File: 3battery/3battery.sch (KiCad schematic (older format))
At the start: 61 parts, among them J1 Barrel_Jack, J2 1 cell, J3 3 cells, J4 opt, J5 opt, J6 opt, Q1 BSL302SNH6327XTSA1, Q2 BSL302SNH6327XTSA1, Q3 CPH6350-TL-W, U1 bq24133, U2 TPS62143

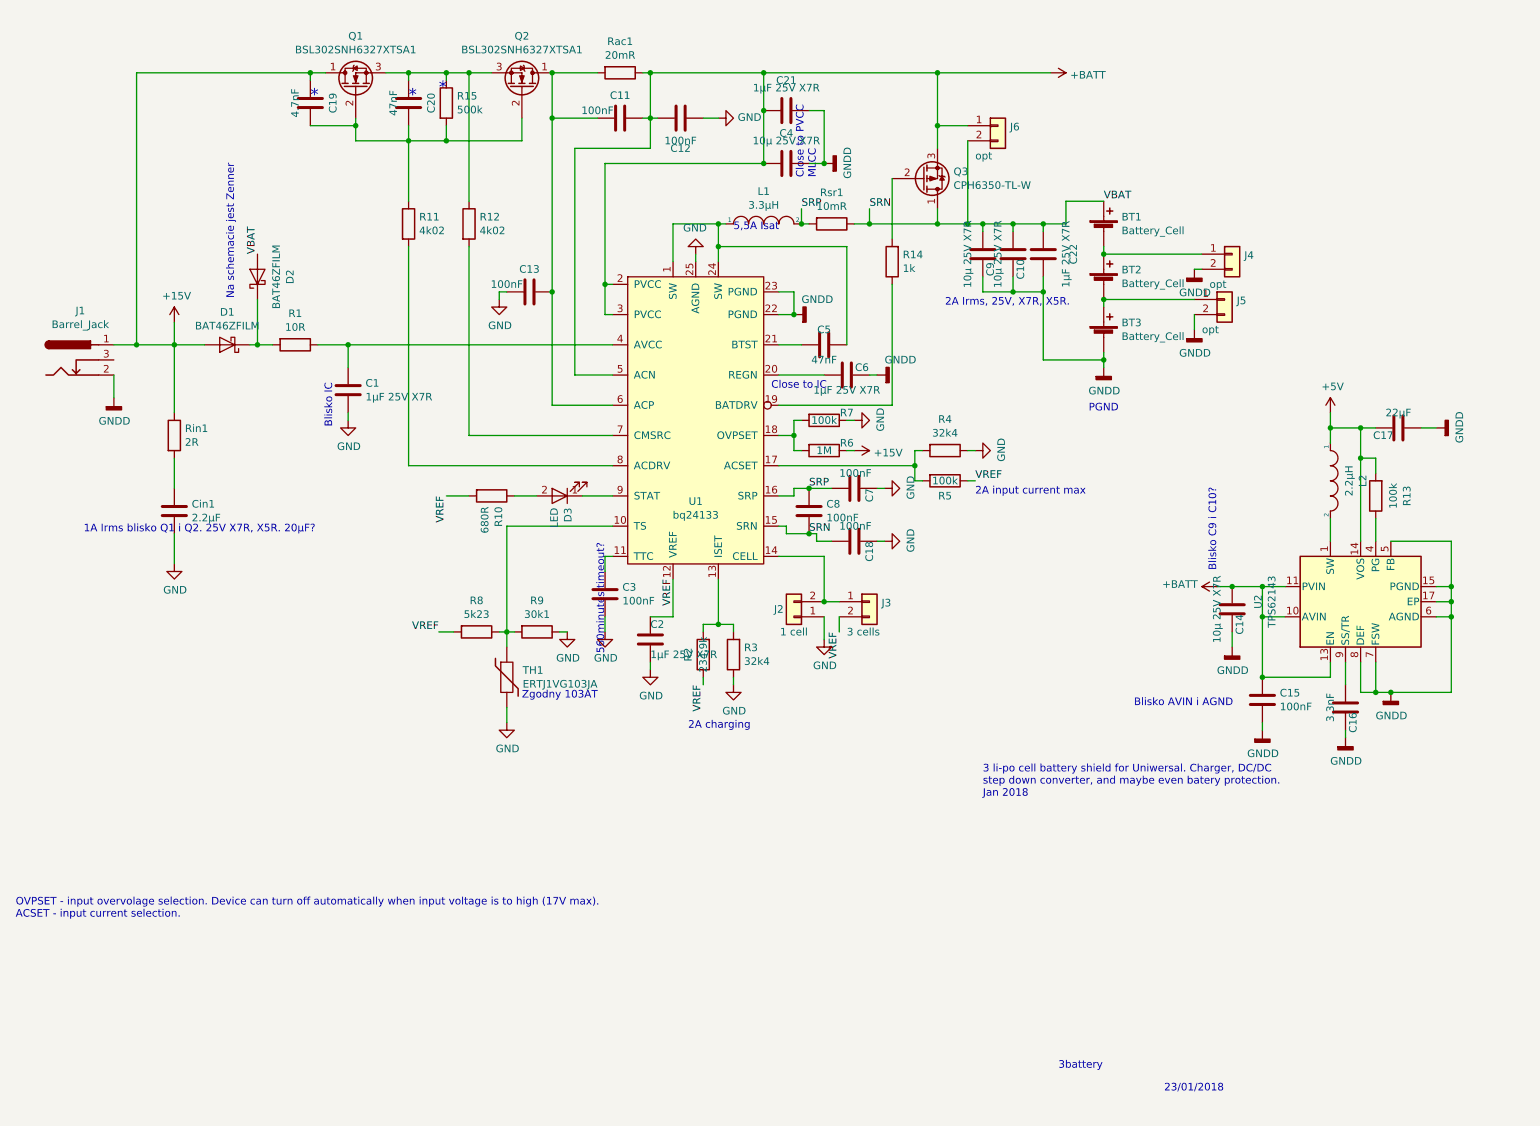
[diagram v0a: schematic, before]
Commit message: Main board and proto-board added
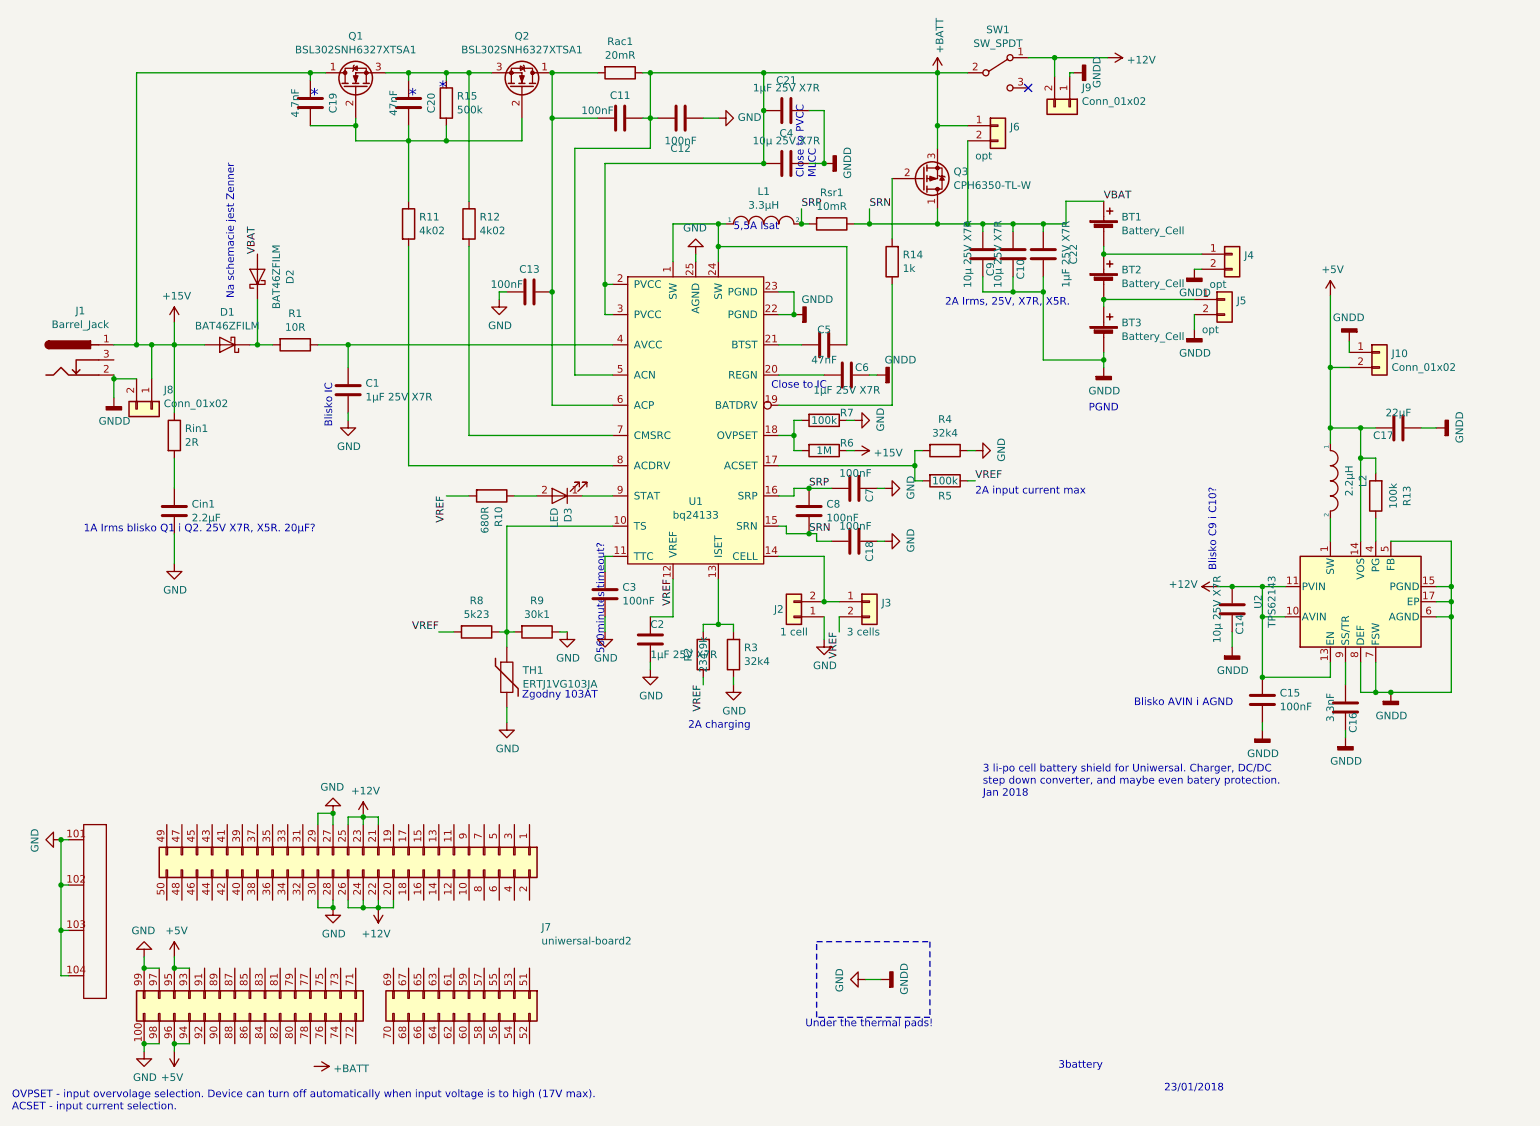
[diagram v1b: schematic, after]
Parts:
- added J10, J8, J9: Conn_01x02, Connector_PinHeader_2.54mm:PinHeader_1x02_P2.54mm_Vertical, symbol Connector_Generic:Conn_01x02
- added J7: uniwersal-board2, iwasz:uniwersal-board, symbol iwasz-kicad:uniwersal-board2
- added SW1: SW_SPDT, Button_Switch_THT:SW_CuK_OS102011MA1QN1_SPDT_Angled, symbol Switch:SW_SPDT
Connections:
- net GNDD is gone; now on net GND: BT3.2 (-), C10.1, C14.1, C15.2, C16.1, C17.2, C21.1, C22.1, C4.1, C6.1, C9.1, J1.2, J4.2 (Pin_2), J5.2 (Pin_2), U1.22 (PGND), U1.23 (PGND), U2.15 (PGND), U2.16 (PGND), U2.17 (EP), U2.5 (FB), U2.6 (AGND), U2.7 (FSW), U2.8 (DEF)
- net +15V: now also J8.1 (Pin_1)
- net +5V: now also J10.2 (Pin_2), J7.93 (Pin_23), J7.94 (Pin_24), J7.95 (Pin_25), J7.96 (Pin_26)
- net +BATT: now also SW1.2 (B); no longer C14.2, C15.1, U2.10 (AVIN), U2.11 (PVIN), U2.12 (PVIN), U2.13 (EN)
- net GND: now also J10.1 (Pin_1), J7.100 (Pin_30), J7.101, J7.102, J7.103, J7.104, J7.27 (Pin_27), J7.28 (Pin_28), J7.29 (Pin_29), J7.30 (Pin_30), J7.97 (Pin_27), J7.98 (Pin_28), J7.99 (Pin_29), J8.2 (Pin_2), J9.1 (Pin_1)
- new net +12V: C14.2, C15.1, J7.20 (Pin_20), J7.21 (Pin_21), J7.22 (Pin_22), J7.23 (Pin_23), J7.24 (Pin_24), J7.25 (Pin_25), J7.26 (Pin_26), J9.2 (Pin_2), SW1.1 (A), U2.10 (AVIN), U2.11 (PVIN), U2.12 (PVIN), U2.13 (EN)
- no-connect marks 0 -> 1
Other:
- note added: "Under the thermal pads!"

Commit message: Gerbers directory added, and domcumentation improved
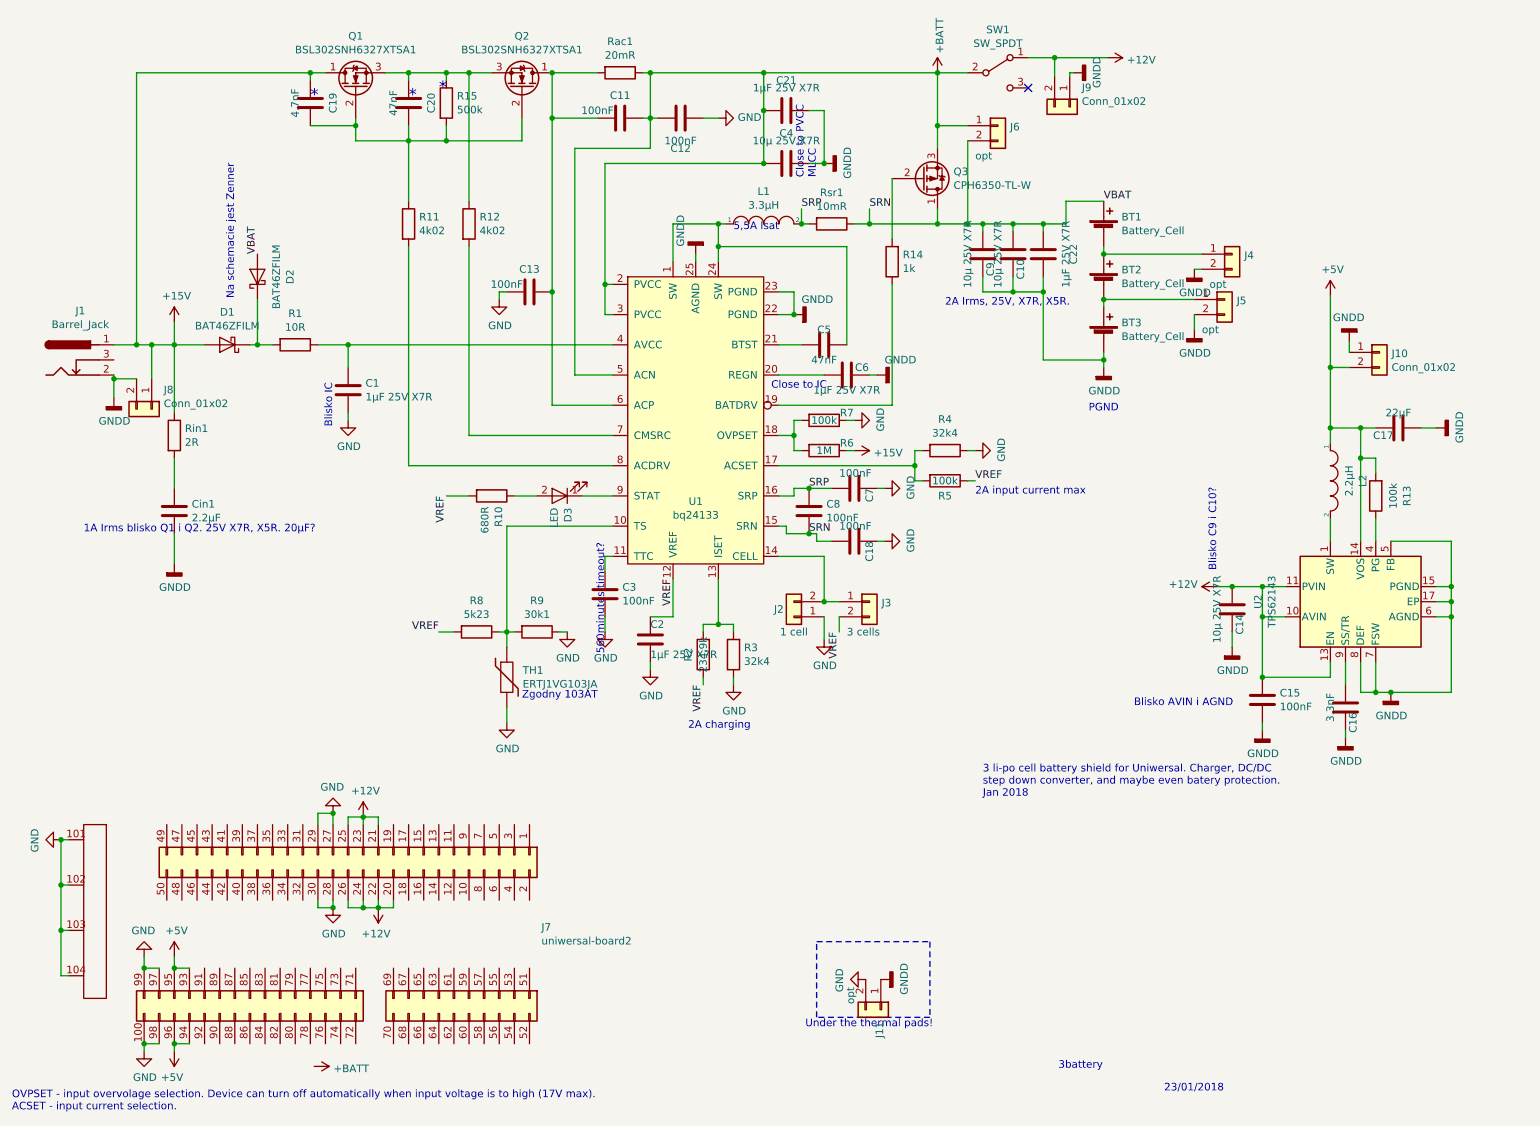
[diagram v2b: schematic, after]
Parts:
- added J11: opt, Resistor_SMD:R_0402_1005Metric, symbol Connector_Generic:Conn_01x02
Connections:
- net GND: now also J11.2 (Pin_2); no longer BT3.2 (-), C10.1, C14.1, C15.2, C16.1, C17.2, C21.1, C22.1, C4.1, C6.1, C9.1, Cin1.2, J1.2, J10.1 (Pin_1), J4.2 (Pin_2), J5.2 (Pin_2), J8.2 (Pin_2), J9.1 (Pin_1), U1.22 (PGND), U1.23 (PGND), U1.25 (AGND), U2.15 (PGND), U2.16 (PGND), U2.17 (EP), U2.5 (FB), U2.6 (AGND), U2.7 (FSW), U2.8 (DEF)
- new net GNDD: BT3.2 (-), C10.1, C14.1, C15.2, C16.1, C17.2, C21.1, C22.1, C4.1, C6.1, C9.1, Cin1.2, J1.2, J10.1 (Pin_1), J11.1 (Pin_1), J4.2 (Pin_2), J5.2 (Pin_2), J8.2 (Pin_2), J9.1 (Pin_1), U1.22 (PGND), U1.23 (PGND), U1.25 (AGND), U2.15 (PGND), U2.16 (PGND), U2.17 (EP), U2.5 (FB), U2.6 (AGND), U2.7 (FSW), U2.8 (DEF)
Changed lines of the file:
@@
-	1    0    0    -1
-$EndComp
-$Comp
-L power:GND #PWR01
-U 1 1 5A673EA2
-P 1600 4150
-F 0 "#PWR01" H 1600 3900 50  0001 C CNN
-F 1 "GND" H 1605 3977 50  0000 C CNN
-F 2 "" H 1600 4150 50  0001 C CNN
-F 3 "" H 1600 4150 50  0001 C CNN
-	1    1600 4150
 	1    0    0    -1
 $EndComp
@@
 F 1 "bq24133" H 5050 2373 50  0000 C CNN
 F 2 "iwasz:R-PVQFN-N24" H 5100 3100 50  0001 C CNN
-F 3 "" H 5100 3100 50  0001 C CNN
+F 3 "http://pl.farnell.com/texas-instruments/bq24133rgyt/batt-charger-li-ion-pol-2-5a-vqfn/dp/2492091" H 5100 3100 50  0001 C CNN
 	1    5050 3100
 	1    0    0    -1
-$EndComp
-$Comp
-L power:GND #PWR03
-U 1 1 5A6785D7
-P 5050 2100
-F 0 "#PWR03" H 5050 1850 50  0001 C CNN
-F 1 "GND" H 5055 1927 50  0000 C CNN
-F 2 "" H 5050 2100 50  0001 C CNN
-F 3 "" H 5050 2100 50  0001 C CNN
-	1    5050 2100
-	-1   0    0    1
 $EndComp
 Wire Wire Line
@@
 	850  6875 900  6875
 Connection ~ 850  6575
-Wire Wire Line
-	6175 6900 6275 6900
+$Comp
+L power:GNDD #PWR01
+U 1 1 5A7F1CC5
+P 1600 4150
+F 0 "#PWR01" H 1600 3900 50  0001 C CNN
+F 1 "GNDD" H 1604 3995 50  0000 C CNN
+F 2 "" H 1600 4150 50  0001 C CNN
+F 3 "" H 1600 4150 50  0001 C CNN
+	1    1600 4150
+	1    0    0    -1
+$EndComp
+$Comp
+L Connector_Generic:Conn_01x02 J11
+U 1 1 5A7C429F
+P 6275 7100
+F 0 "J11" H 6355 7092 50  0000 L CNN
+F 1 "opt" H 6125 6900 50  0000 L CNN
+F 2 "Resistor_SMD:R_0402_1005Metric" H 6275 7100 50  0001 C CNN
+F 3 "~" H 6275 7100 50  0001 C CNN
+	1    6275 7100
+	0    1    1    0
+$EndComp
+$Comp
+L power:GNDD #PWR03
+U 1 1 5A7C6993
+P 5050 2100
+F 0 "#PWR03" H 5050 1850 50  0001 C CNN
+F 1 "GNDD" V 5150 2050 50  0000 R CNN
+F 2 "" H 5050 2100 50  0001 C CNN
+F 3 "" H 5050 2100 50  0001 C CNN
+	1    5050 2100
+	-1   0    0    1
+$EndComp
 $EndSCHEMATC

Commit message: Bug-fixes. 3 battery soldered and working.
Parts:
- added D4: LED, Diode_SMD:D_0805_2012Metric, symbol Device:LED
- added R16: 680R, Resistor_SMD:R_0603_1608Metric, symbol Device:R
- added Rin2: 3.9, Resistor_SMD:R_2010_5025Metric, symbol Device:R
- J3: footprint Jumper:SolderJumper-2_P1.3mm_Open_RoundedPad1.0x1.5mm -> Jumper:SolderJumper-2_P1.3mm_Bridged_RoundedPad1.0x1.5mm
- R10: value 680R -> 560
- Rin1: value 2R -> 3.9
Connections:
- net +15V: now also Rin2.1
- net +5V: now also R16.2
- net GNDD: now also D4.1 (K)
- net at Cin1.1, Rin1.2: now also Rin2.2
- new net: D4.2 (A), R16.1
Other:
- note added: "TODO po co to było!?"
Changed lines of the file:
@@
 U 1 1 5A673CEE
 P 1600 3300
-F 0 "Rin1" H 1670 3346 50  0000 L CNN
-F 1 "2R" H 1670 3255 50  0000 L CNN
+F 0 "Rin1" H 1375 3325 50  0000 L CNN
+F 1 "3.9" H 1425 3250 50  0000 L CNN
 F 2 "Resistor_SMD:R_2010_5025Metric" V 1530 3300 50  0001 C CNN
 F 3 "" H 1600 3300 50  0001 C CNN
@@
 	1200 2700 1350 2700
 Wire Wire Line
-	1600 3450 1600 3650
+	1600 3450 1600 3525
 Wire Wire Line
 	1600 3950 1600 4150
@@
 P 3700 3700
 F 0 "R10" H 3770 3746 50  0000 L CNN
-F 1 "680R" H 3770 3655 50  0000 L CNN
+F 1 "560" H 3770 3655 50  0000 L CNN
 F 2 "Resistor_SMD:R_0603_1608Metric" V 3630 3700 50  0001 C CNN
 F 3 "" H 3700 3700 50  0001 C CNN
@@
 	4450 4500 4450 4600
 Wire Wire Line
-	1600 2700 1600 3150
+	1600 2700 1600 3050
 Connection ~ 1600 2700
 $Comp
@@
 P 4750 4650
 F 0 "C2" H 4750 4750 50  0000 L CNN
-F 1 "1µF 25V X7R" H 4750 4550 50  0000 L CNN
+F 1 "1µF 25V X7R" V 4625 4225 50  0000 L CNN
 F 2 "Capacitor_SMD:C_0805_2012Metric" H 4788 4500 50  0001 C CNN
 F 3 "" H 4750 4650 50  0001 C CNN
@@
 F 0 "J3" H 6280 4392 50  0000 L CNN
 F 1 "3 cells" H 6050 4200 50  0000 L CNN
-F 2 "Jumper:SolderJumper-2_P1.3mm_Open_RoundedPad1.0x1.5mm" H 6200 4400 50  0001 C CNN
+F 2 "Jumper:SolderJumper-2_P1.3mm_Bridged_RoundedPad1.0x1.5mm" H 6200 4400 50  0001 C CNN
 F 3 "~" H 6200 4400 50  0001 C CNN
 	1    6200 4400
@@
 L power:+5V #PWR028
 U 1 1 5A6DF896
-P 9250 2375
-F 0 "#PWR028" H 9250 2225 50  0001 C CNN
-F 1 "+5V" H 9265 2548 50  0000 C CNN
-F 2 "" H 9250 2375 50  0001 C CNN
-F 3 "" H 9250 2375 50  0001 C CNN
-	1    9250 2375
+P 9250 2050
+F 0 "#PWR028" H 9250 1900 50  0001 C CNN
+F 1 "+5V" H 9265 2223 50  0000 C CNN
+F 2 "" H 9250 2050 50  0001 C CNN
+F 3 "" H 9250 2050 50  0001 C CNN
+	1    9250 2050
 	1    0    0    -1
 $EndComp
@@
 	9850 3250 9950 3250
 Wire Wire Line
-	9250 2375 9250 2850
+	9250 2050 9250 2225
 Wire Wire Line
 	9550 3250 9450 3250
@@
 L power:+BATT #PWR033
 U 1 1 5A818E7C
-P 2525 7475
-F 0 "#PWR033" H 2525 7325 50  0001 C CNN
-F 1 "+BATT" V 2540 7603 50  0000 L CNN
-F 2 "" H 2525 7475 50  0001 C CNN
-F 3 "" H 2525 7475 50  0001 C CNN
-	1    2525 7475
+P 1375 5325
+F 0 "#PWR033" H 1375 5175 50  0001 C CNN
+F 1 "+BATT" V 1300 5300 50  0000 L CNN
+F 2 "" H 1375 5325 50  0001 C CNN
+F 3 "" H 1375 5325 50  0001 C CNN
+	1    1375 5325
 	0    1    1    0
 $EndComp
@@
 P 1450 3125
 F 0 "J8" V 1323 3205 50  0000 L CNN
-F 1 "Conn_01x02" V 1414 3205 50  0000 L CNN
+F 1 "Conn_01x02" H 1050 3075 50  0000 L CNN
 F 2 "Connector_PinHeader_2.54mm:PinHeader_1x02_P2.54mm_Vertical" H 1450 3125 50  0001 C CNN
 F 3 "~" H 1450 3125 50  0001 C CNN
@@
 	-1   0    0    1
 $EndComp
+Text Notes 1175 5175 0    50   ~ 0
+TODO po co to było!?
+$Comp
+L Device:LED D4
+U 1 1 5ACC4465
+P 10000 2225
+F 0 "D4" V 9945 2303 50  0000 L CNN
+F 1 "LED" V 10036 2303 50  0000 L CNN
+F 2 "Diode_SMD:D_0805_2012Metric" H 10000 2225 50  0001 C CNN
+F 3 "~" H 10000 2225 50  0001 C CNN
+	1    10000 2225
+	-1   0    0    1
+$EndComp
+$Comp
+L Device:R R16
+U 1 1 5ACC446B
+P 9550 2225
+F 0 "R16" H 9620 2271 50  0000 L CNN
+F 1 "680R" H 9620 2180 50  0000 L CNN
+F 2 "Resistor_SMD:R_0603_1608Metric" V 9480 2225 50  0001 C CNN
+F 3 "" H 9550 2225 50  0001 C CNN
+	1    9550 2225
+	0    1    1    0
+$EndComp
+Wire Wire Line
+	9250 2225 9400 2225
+Wire Wire Line
+	9700 2225 9850 2225
+Wire Wire Line
+	10150 2225 10350 2225
+Connection ~ 9250 2225
+Wire Wire Line
+	9250 2225 9250 2850
+$Comp
+L power:GNDD #PWR0101
+U 1 1 5ACFC559
+P 10350 2225
+F 0 "#PWR0101" H 10350 1975 50  0001 C CNN
+F 1 "GNDD" H 10354 2070 50  0000 C CNN
+F 2 "" H 10350 2225 50  0001 C CNN
+F 3 "" H 10350 2225 50  0001 C CNN
+	1    10350 2225
+	0    -1   -1   0
+$EndComp
+$Comp
+L Device:R Rin2
+U 1 1 5AD01686
+P 1775 3300
+F 0 "Rin2" H 1825 3325 50  0000 L CNN
+F 1 "3.9" H 1845 3255 50  0000 L CNN
+F 2 "Resistor_SMD:R_2010_5025Metric" V 1705 3300 50  0001 C CNN
+F 3 "" H 1775 3300 50  0001 C CNN
+	1    1775 3300
+	1    0    0    -1
+$EndComp
+Wire Wire Line
+	1600 3050 1775 3050
+Wire Wire Line
+	1775 3050 1775 3150
+Connection ~ 1600 3050
+Wire Wire Line
+	1600 3050 1600 3150
+Wire Wire Line
+	1775 3450 1775 3525
+Wire Wire Line
+	1775 3525 1600 3525
+Connection ~ 1600 3525
+Wire Wire Line
+	1600 3525 1600 3650
 $EndSCHEMATC
